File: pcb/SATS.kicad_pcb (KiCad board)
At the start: 2 copper layers, 27 parts, among them J1 Raspberry_Pi_2_3, J10 EXT_GPIO, J11 EXT_GPIO, J12 EXT_GPIO, J13 EXT_GPIO, J2 A00-432-262-450, J3 AudioJack4_SwitchTR1, J4 5V, J5 3.3V, J6 Card LED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

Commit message: neatify and reorganize
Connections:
- J2 pad A1: PD_11 -> PD_21
- J2 pad A2: PD_12 -> PD_22
- J2 pad A3: PD_13 -> PD_23
- J2 pad A4: PD_14 -> PD_24
- J2 pad A5: PD_15 -> PD_25
- J2 pad A8: LED1 Out -> LED2 Out
- J2 pad B1: PD_21 -> PD_11
- J2 pad B2: PD_22 -> PD_12
- J2 pad B3: PD_23 -> PD_13
- J2 pad B4: PD_24 -> PD_14
- J2 pad B5: PD_25 -> PD_15
- J2 pad B8: LED2 Out -> LED1 Out
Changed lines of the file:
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@@
     (pad "" np_thru_hole circle locked (at 54.8386 10.033 180) (size 1.6002 1.6002) (drill 1.6002) (layers *.Cu *.Mask))
     (pad "A1" thru_hole circle locked (at 0 0 90) (size 1.397 1.397) (drill 0.889) (layers *.Cu *.Mask)
-      (net 33 "PD_11") (pinfunction "A1") (pintype "unspecified"))
+      (net 39 "PD_21") (pinfunction "A1") (pintype "unspecified"))
     (pad "A2" thru_hole circle locked (at 1.27 -2.54 90) (size 1.397 1.397) (drill 0.889) (layers *.Cu *.Mask)
-      (net 34 "PD_12") (pinfunction "A2") (pintype "unspecified"))
+      (net 40 "PD_22") (pinfunction "A2") (pintype "unspecified"))
     (pad "A3" thru_hole circle locked (at 2.54 0 90) (size 1.397 1.397) (drill 0.889) (layers *.Cu *.Mask)
-      (net 35 "PD_13") (pinfunction "A3") (pintype "unspecified"))
+      (net 41 "PD_23") (pinfunction "A3") (pintype "unspecified"))
     (pad "A4" thru_hole circle locked (at 3.81 -2.54 90) (size 1.397 1.397) (drill 0.889) (layers *.Cu *.Mask)
-      (net 36 "PD_14") (pinfunction "A4") (pintype "unspecified"))
+      (net 42 "PD_24") (pinfunction "A4") (pintype "unspecified"))
     (pad "A5" thru_hole circle locked (at 5.08 0 90) (size 1.397 1.397) (drill 0.889) (layers *.Cu *.Mask)
-      (net 37 "PD_15") (pinfunction "A5") (pintype "unspecified"))
+      (net 43 "PD_25") (pinfunction "A5") (pintype "unspecified"))
     (pad "A6" thru_hole circle locked (at 6.35 -2.54 90) (size 1.397 1.397) (drill 0.889) (layers *.Cu *.Mask)
       (net 3 "+5V") (pinfunction "A6") (pintype "unspecified"))
@@
       (net 2 "Earth") (pinfunction "A7") (pintype "unspecified"))
     (pad "A8" thru_hole circle locked (at 8.89 -2.54 90) (size 1.397 1.397) (drill 0.889) (layers *.Cu *.Mask)
-      (net 38 "LED1 Out") (pinfunction "A8") (pintype "unspecified"))
+      (net 44 "LED2 Out") (pinfunction "A8") (pintype "unspecified"))
     (pad "B1" thru_hole circle locked (at 13.97 0 90) (size 1.397 1.397) (drill 0.889) (layers *.Cu *.Mask)
-      (net 39 "PD_21") (pinfunction "B1") (pintype "unspecified"))
+      (net 33 "PD_11") (pinfunction "B1") (pintype "unspecified"))
     (pad "B2" thru_hole circle locked (at 15.24 -2.54 90) (size 1.397 1.397) (drill 0.889) (layers *.Cu *.Mask)
-      (net 40 "PD_22") (pinfunction "B2") (pintype "unspecified"))
+      (net 34 "PD_12") (pinfunction "B2") (pintype "unspecified"))
     (pad "B3" thru_hole circle locked (at 16.51 0 90) (size 1.397 1.397) (drill 0.889) (layers *.Cu *.Mask)
-      (net 41 "PD_23") (pinfunction "B3") (pintype "unspecified"))
+      (net 35 "PD_13") (pinfunction "B3") (pintype "unspecified"))
     (pad "B4" thru_hole circle locked (at 17.78 -2.54 90) (size 1.397 1.397) (drill 0.889) (layers *.Cu *.Mask)
-      (net 42 "PD_24") (pinfunction "B4") (pintype "unspecified"))
+      (net 36 "PD_14") (pinfunction "B4") (pintype "unspecified"))
     (pad "B5" thru_hole circle locked (at 19.05 0 90) (size 1.397 1.397) (drill 0.889) (layers *.Cu *.Mask)
-      (net 43 "PD_25") (pinfunction "B5") (pintype "unspecified"))
+      (net 37 "PD_15") (pinfunction "B5") (pintype "unspecified"))
     (pad "B6" thru_hole circle locked (at 20.32 -2.54 90) (size 1.397 1.397) (drill 0.889) (layers *.Cu *.Mask)
       (net 3 "+5V") (pinfunction "B6") (pintype "unspecified"))
@@
       (net 2 "Earth") (pinfunction "B7") (pintype "unspecified"))
     (pad "B8" thru_hole circle locked (at 22.86 -2.54 90) (size 1.397 1.397) (drill 0.889) (layers *.Cu *.Mask)
-      (net 44 "LED2 Out") (pinfunction "B8") (pintype "unspecified"))
+      (net 38 "LED1 Out") (pinfunction "B8") (pintype "unspecified"))
     (pad "C1" thru_hole circle locked (at 27.94 0 90) (size 1.397 1.397) (drill 0.889) (layers *.Cu *.Mask)
       (net 45 "PD_31") (pinfunction "C1") (pintype "unspecified"))

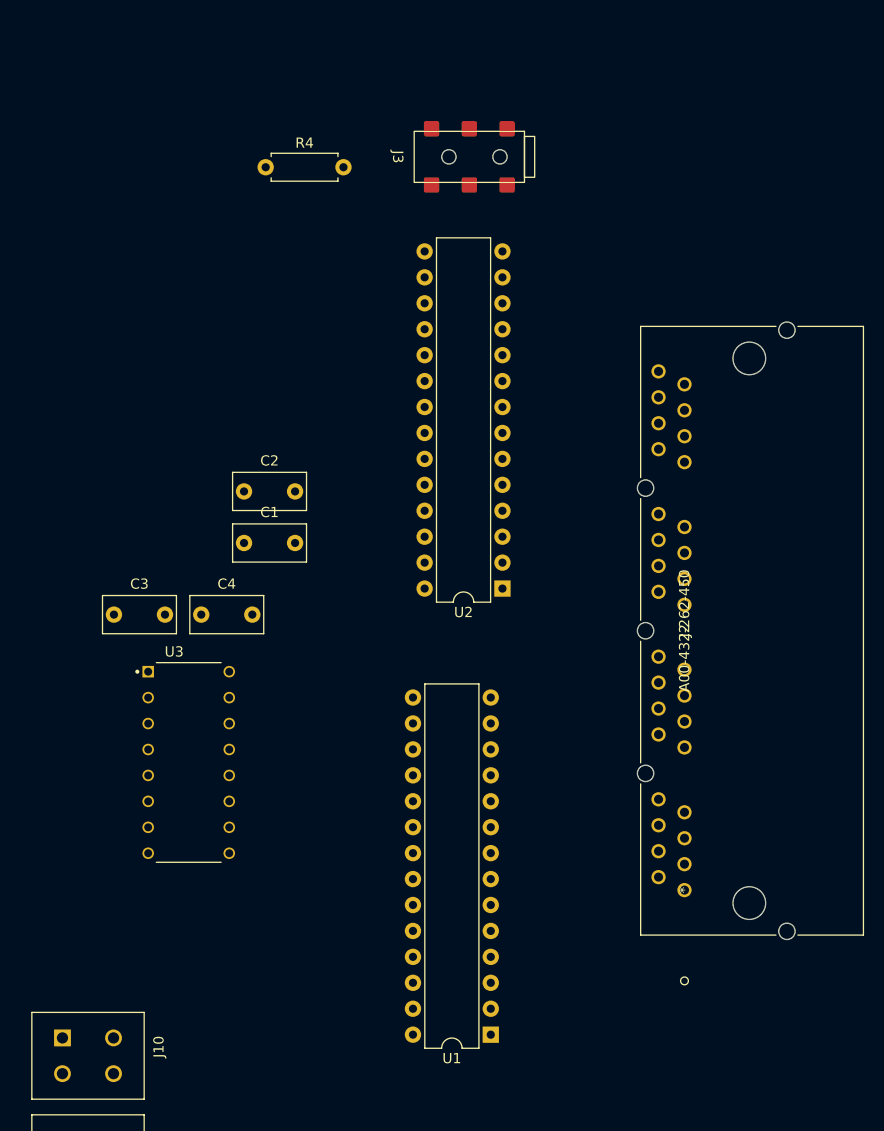
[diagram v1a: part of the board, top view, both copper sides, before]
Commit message: Route PD lines
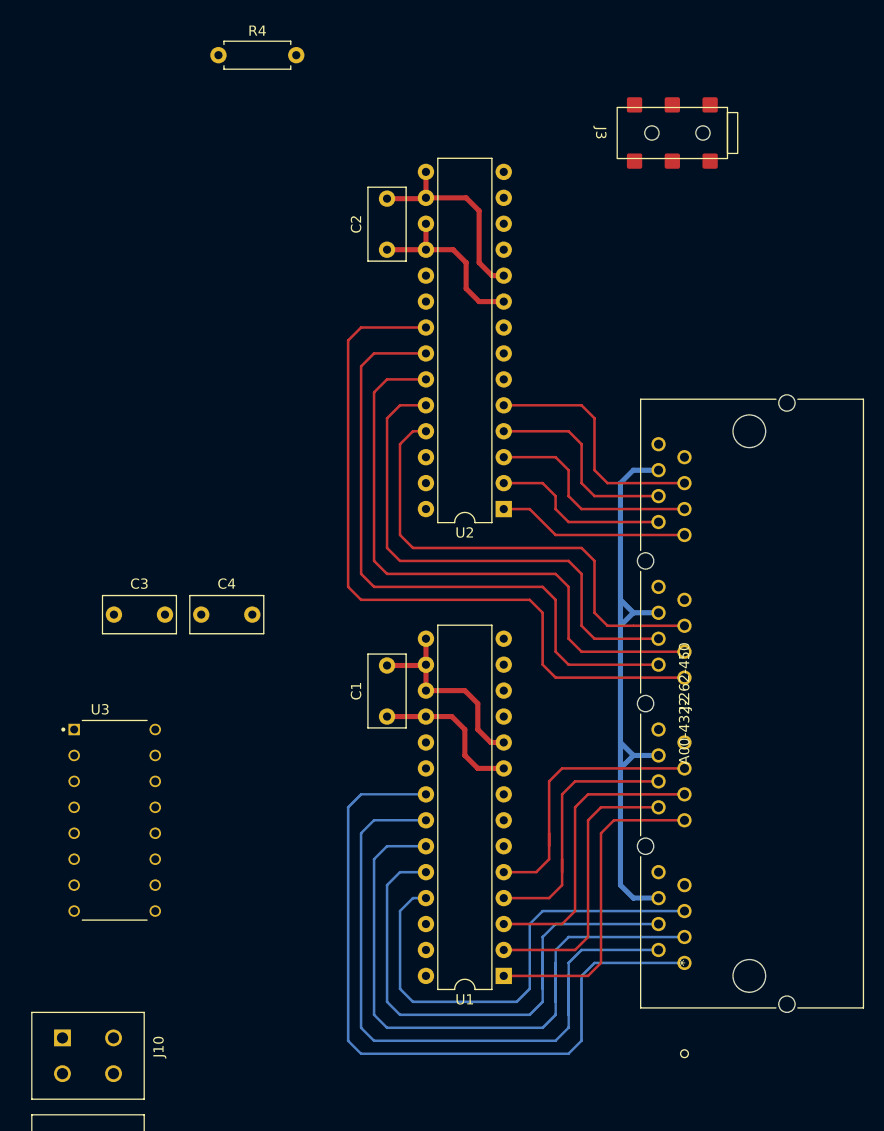
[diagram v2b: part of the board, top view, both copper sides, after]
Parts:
- moved C2 27.5 mm to (170.2, 76.2), turned to 90 degrees
- moved C1 22.0 mm to (170.2, 121.9), turned to 90 degrees
- moved J3 20.0 mm to (198.1, 64.8)
- moved R4 11.9 mm to (153.7, 57.1)
- moved U3 9.20 mm to (143.5, 132.1)
- moved U2 7.79 mm to (181.6, 101.6)
- moved J2 7.13 mm to (199.3, 146.1)
- moved U1 5.89 mm to (181.6, 147.3)
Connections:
- J2 pad C1: PD_31 -> PD_41
- J2 pad C2: PD_32 -> PD_42
- J2 pad C3: PD_33 -> PD_43
- J2 pad C4: PD_34 -> PD_44
- J2 pad C5: PD_35 -> PD_45
- J2 pad D1: PD_41 -> PD_31
- J2 pad D2: PD_42 -> PD_32
- J2 pad D3: PD_43 -> PD_33
- J2 pad D4: PD_44 -> PD_34
- J2 pad D5: PD_45 -> PD_35
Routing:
- net PD_41: track 0.00 -> 71.9 mm
- net PD_21: track 0.00 -> 71.9 mm
- net PD_22: track 0.00 -> 66.8 mm
- net PD_42: track 0.00 -> 63.0 mm
- net PD_23: track 0.00 -> 63.0 mm
- net +5V: track 0.00 -> 60.0 mm
- net PD_43: track 0.00 -> 59.2 mm
- net PD_24: track 0.00 -> 54.1 mm
- net PD_44: track 0.00 -> 50.3 mm
- net PD_25: track 0.00 -> 46.5 mm
- net PD_45: track 0.00 -> 46.5 mm
- net Earth: track 0.00 -> 40.3 mm
- net +3V3: track 0.00 -> 32.6 mm
- net PD_11: track 0.00 -> 31.5 mm
- net PD_13: track 0.00 -> 28.9 mm
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
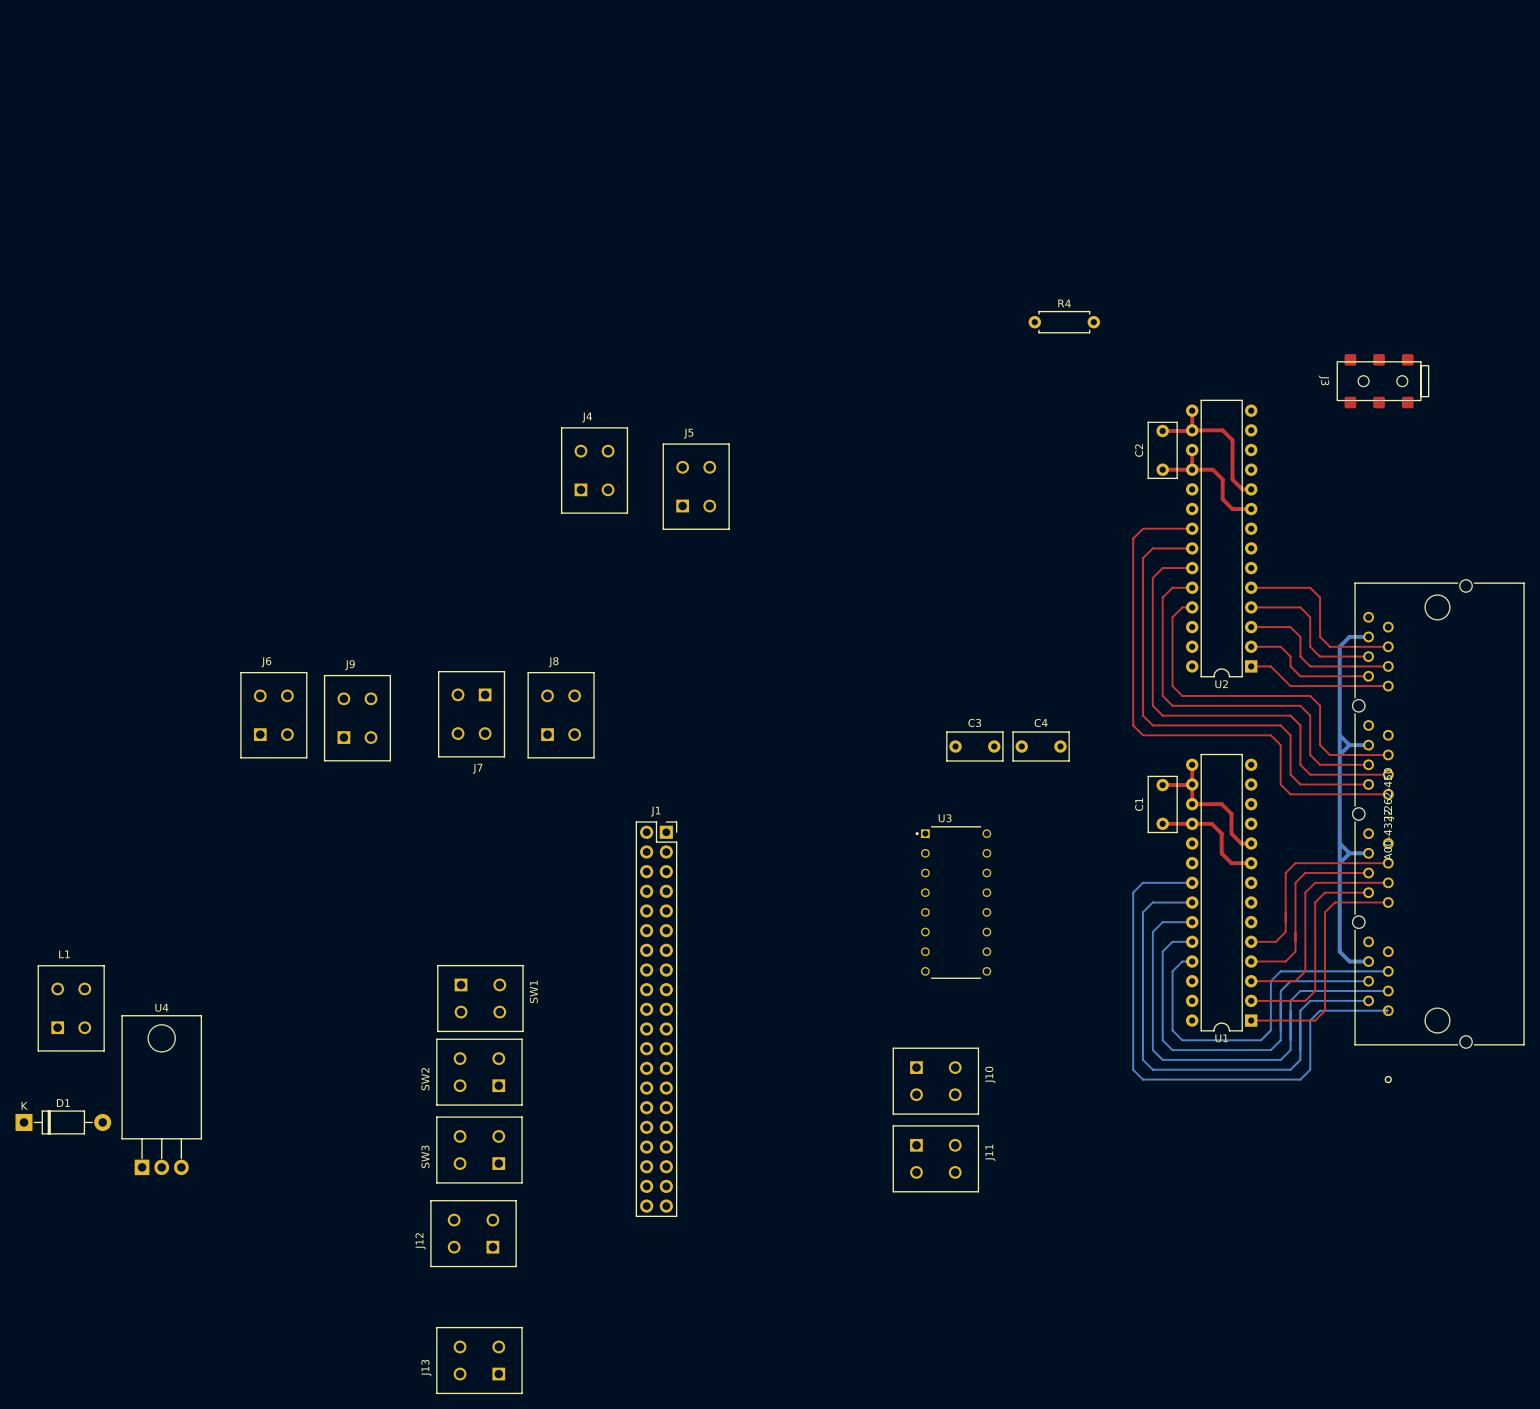
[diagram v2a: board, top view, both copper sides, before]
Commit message: Clead PD Lines and route LED Outs
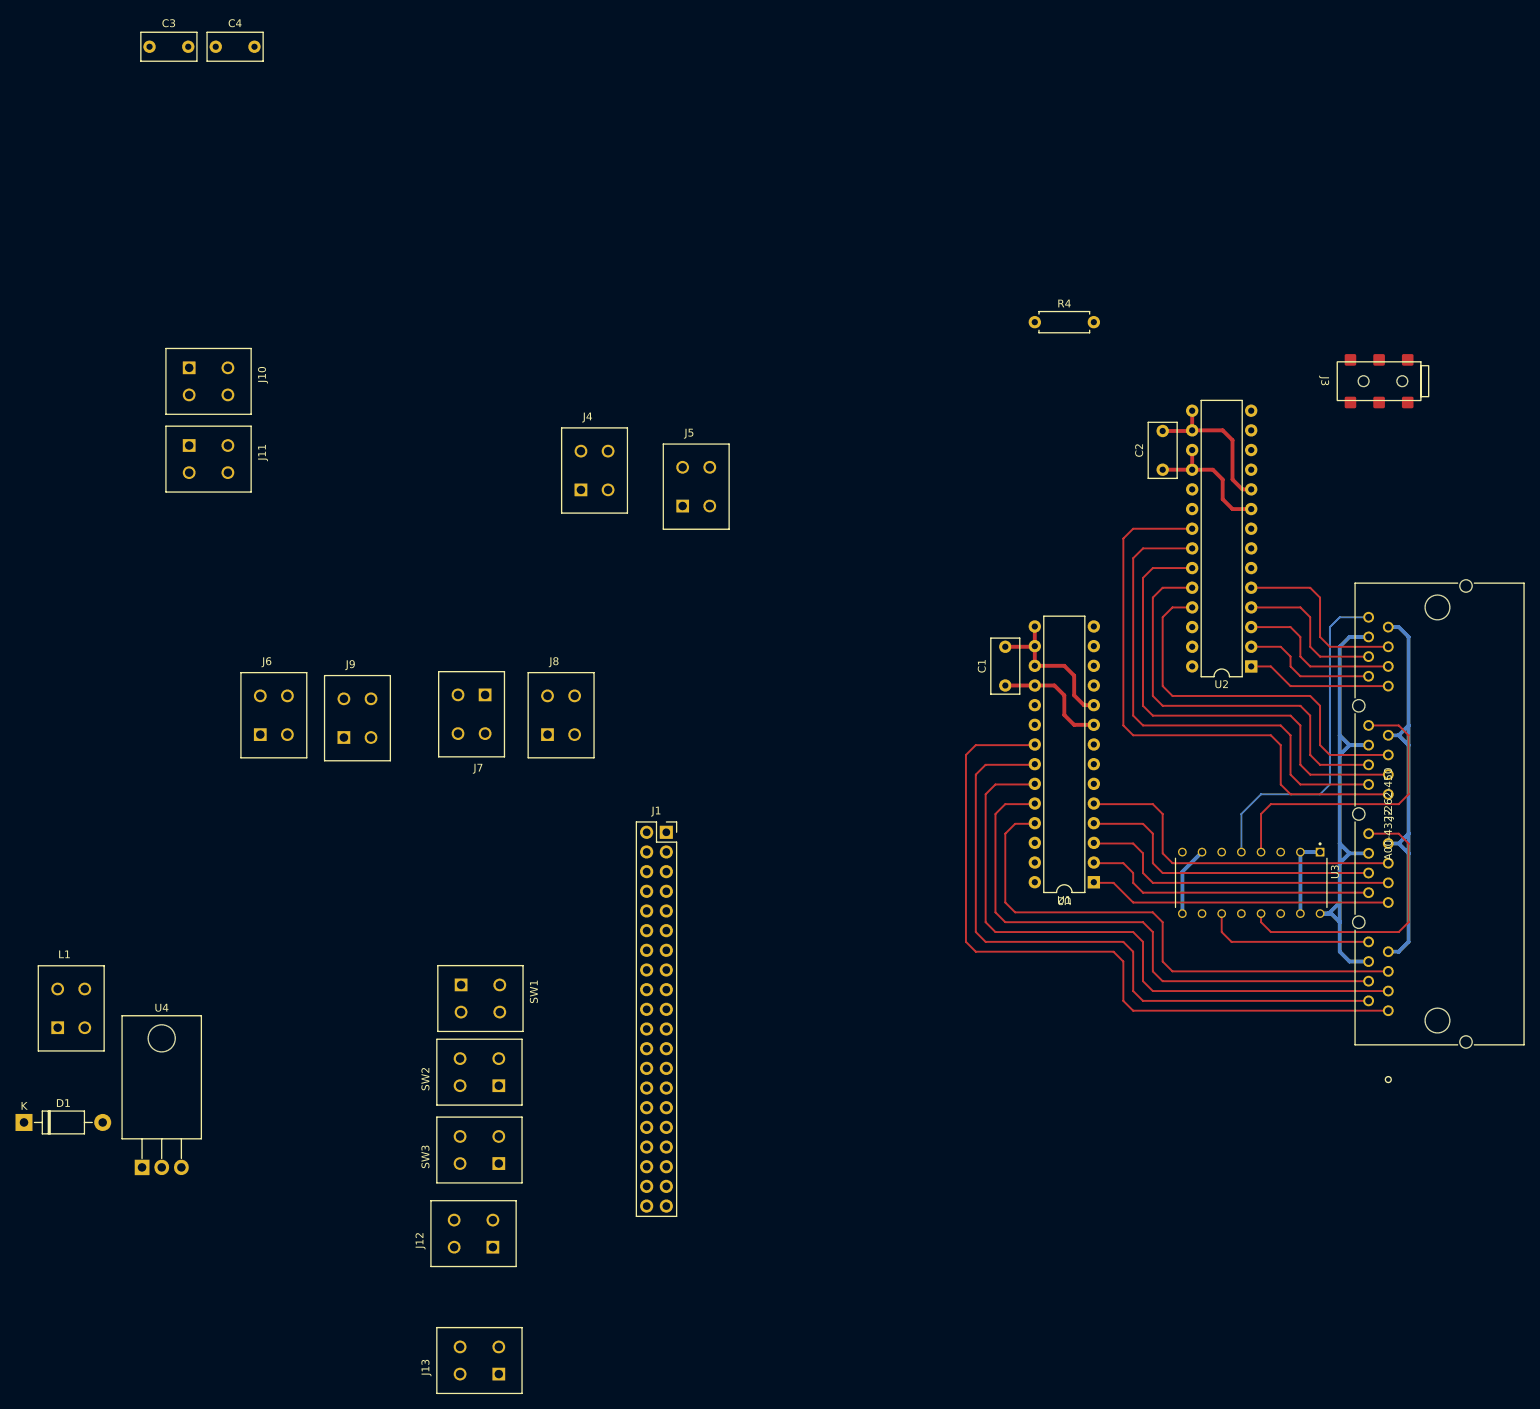
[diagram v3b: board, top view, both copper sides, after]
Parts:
- moved C3 137.8 mm to (39.4, 21.6)
- moved C4 137.8 mm to (47.9, 21.6)
- moved J10 130.3 mm to (47.0, 64.8)
- moved J11 130.3 mm to (47.0, 74.8)
- moved U3 38.2 mm to (181.6, 129.5), turned to -90 degrees
- moved U1 27.1 mm to (161.3, 129.5)
- moved C1 27.1 mm to (149.9, 104.1)
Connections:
- U3 pad 10: LED Sig1 -> LED Sig2
- U3 pad 11: LED1 Out -> LED2 Out
- U3 pad 13: LED3 Out -> LED1 Out
- U3 pad 14: LED Sig3 -> LED Sig1
- U3 pad 3: LED Sig4 -> LED Sig3
- U3 pad 4: LED4 Out -> LED3 Out
- U3 pad 5: LED2 Out -> LED4 Out
- U3 pad 6: LED Sig2 -> LED Sig4
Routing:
- net Earth: track 40.3 -> 95.8 mm
- net LED4 Out: track 0.00 -> 43.8 mm
- net LED3 Out: track 0.00 -> 38.3 mm
- net LED1 Out: track 0.00 -> 37.1 mm
- net PD_21: track 71.9 -> 94.7 mm
- net PD_25: track 46.5 -> 69.3 mm
- net LED2 Out: track 0.00 -> 21.9 mm
- net +3V3: track 32.6 -> 52.1 mm
- net PD_24: track 54.1 -> 73.1 mm
- net PD_23: track 63.0 -> 82.0 mm
- net PD_22: track 66.8 -> 85.8 mm
- net PD_15: track 27.6 -> 44.2 mm
- net PD_14: track 26.4 -> 40.3 mm
- net PD_13: track 28.9 -> 41.6 mm
- net PD_12: track 27.6 -> 37.8 mm
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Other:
- board text added: "U2"

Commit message: mostly done
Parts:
- J1: moved to B.Cu
- moved J3 159.1 mm to (55.1, 134.6), turned to 90 degrees
- moved J2 156.2 mm to (66.3, 64.2), turned to -90 degrees
- moved J10 116.4 mm to (152.2, 114.5)
- moved J11 115.1 mm to (152.2, 121.5)
- moved D1 114.1 mm to (133.9, 133.0), turned to 180 degrees
- moved R4 110.7 mm to (69.5, 129.0)
- moved U3 108.9 mm to (84.3, 80.7), turned to 90 degrees
- moved J9 103.9 mm to (152.2, 50.0), turned to 90 degrees
- moved J6 103.6 mm to (152.2, 71.0), turned to 90 degrees
- moved L1 99.3 mm to (128.5, 142.5), turned to 180 degrees
- moved U2 97.5 mm to (84.3, 108.6), turned to 0 degrees
- moved SW3 95.2 mm to (152.2, 99.8)
- moved C2 94.3 mm to (95.8, 134.0), turned to -90 degrees
- moved SW2 93.2 mm to (152.2, 92.8)
- moved SW1 91.5 mm to (152.2, 85.8), turned to 90 degrees
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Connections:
- J1 pad 19: LED Sig1 -> LED Sig2
- J1 pad 21: LED Sig2 -> LED Sig4
- J1 pad 23: LED Sig3 -> LED Sig1
- J1 pad 27: LED Sig4 -> LED Sig3
- J11 pad 1: EXT_GPIO13 -> EXT_GPIO12
- J11 pad 2: EXT_GPIO13 -> EXT_GPIO12
- J11 pad 3: EXT_GPIO19 -> EXT_GPIO13
- J11 pad 4: EXT_GPIO19 -> EXT_GPIO13
- J12 pad 3: EXT_GPIO12 -> EXT_GPIO19
- J12 pad 4: EXT_GPIO12 -> EXT_GPIO19
- J7 pad 1: Wiegand 0 -> Wiegand 1
- J7 pad 2: Wiegand 0 -> Wiegand 1
- J7 pad 3: Wiegand 1 -> Wiegand 0
- J7 pad 4: Wiegand 1 -> Wiegand 0
- J9 pad 1: +5V -> Earth
- J9 pad 2: +5V -> Earth
- J9 pad 3: Earth -> +5V
- J9 pad 4: Earth -> +5V
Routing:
- net Earth: track 95.8 -> 669.9 mm, vias 0 -> 1
- net +5V: track 66.1 -> 384.8 mm, vias 0 -> 2
- net +3V3: track 52.1 -> 228.0 mm, vias 0 -> 2
- net SCL: track 0.00 -> 129.8 mm
- net SDA: track 0.00 -> 128.3 mm
- net 1-Wire: track 0.00 -> 119.3 mm
- net LED Sig1: track 0.00 -> 106.1 mm
- net LED Sig2: track 0.00 -> 101.8 mm
- net LED Sig3: track 0.00 -> 97.0 mm
- net LED Sig4: track 0.00 -> 94.6 mm
- net Int 2A: track 0.00 -> 76.6 mm, vias 0 -> 1
- net Int 2B: track 0.00 -> 75.6 mm, vias 0 -> 1
- net Latch: track 0.00 -> 55.0 mm
- net Int 1A: track 0.00 -> 45.0 mm
- net EXT_GPIO19: track 0.00 -> 43.0 mm
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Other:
- board outline added: 108.5 x 103.4 mm
- board text added: "3RD"
- board text added: "3V3"
- board text added: "5V"
- board text added: "BEEP"
- board text added: "DOOR"
- board text added: "GND"
- board text added: "GRN"
- board text added: "IO05"
- board text added: "IO06"
- board text added: "IO12"
- board text added: "IO13"
- board text added: "IO16"
- board text added: "IO19"
- board text added: "IO20"
- board text added: "IO21"
- board text added: "LATCH"
- board text added: "RED"
- board text added: "SERV"
- board text added: "W0"
- board text added: "W1"
- board text removed: "U2"
